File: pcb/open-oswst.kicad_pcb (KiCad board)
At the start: 2 copper layers, 70 x 50 mm, 16 parts

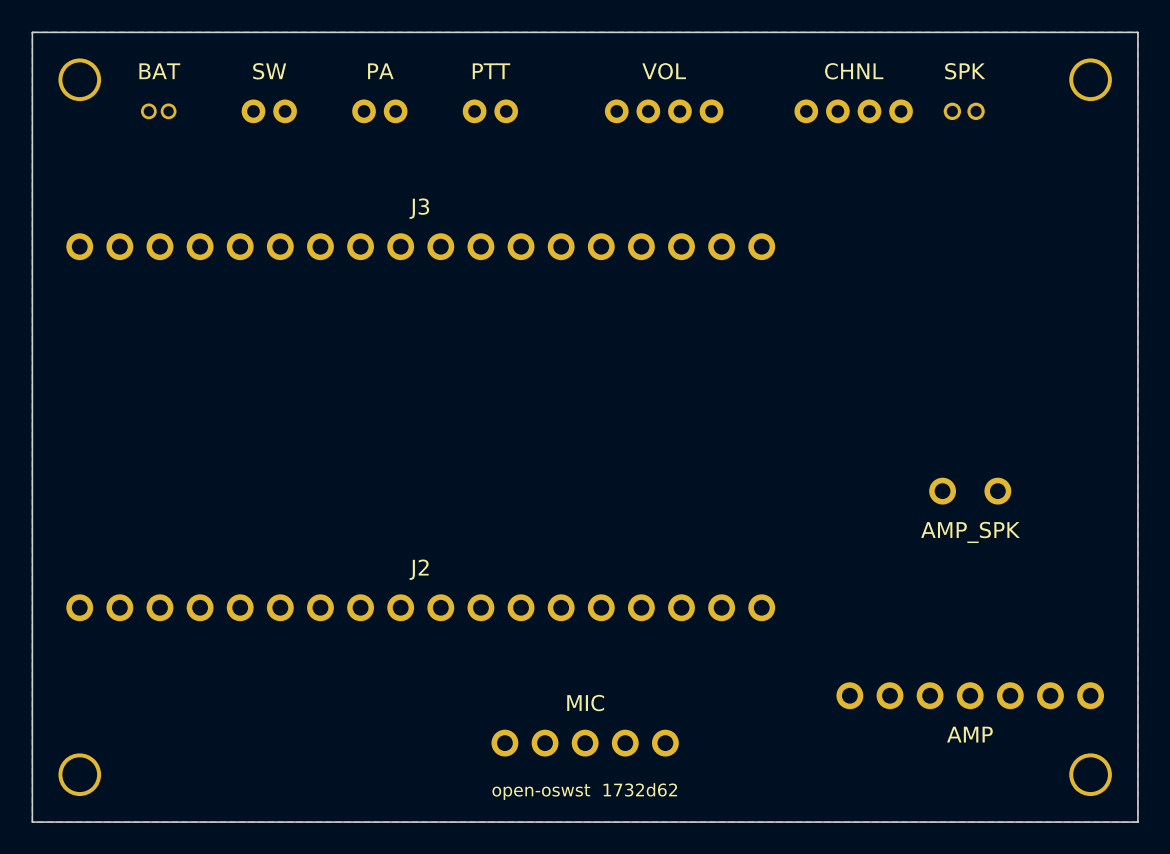
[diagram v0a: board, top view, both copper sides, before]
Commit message: PCB: fix connector types and MIC pin order
- BAT: JST-SH → JST-PH (2.0mm, standard LiPo connector)
- SPK: JST-PH → JST-ZH (1.5mm, matches speaker connector)
- Flip SPK pin order to uncross traces
- Fix MIC header pin order to match actual board (GND,VDD,GAIN,OUT,AR)
- Reduce thermal gap/bridge to 0.3mm to fix DRC spoke errors
- Add add_text() and add_jst_zh() to PCB DSL
- Switch paper to USLetter for 1:1 printing

Co-Authored-By: Claude Opus 4.6 <noreply@anthropic.com>
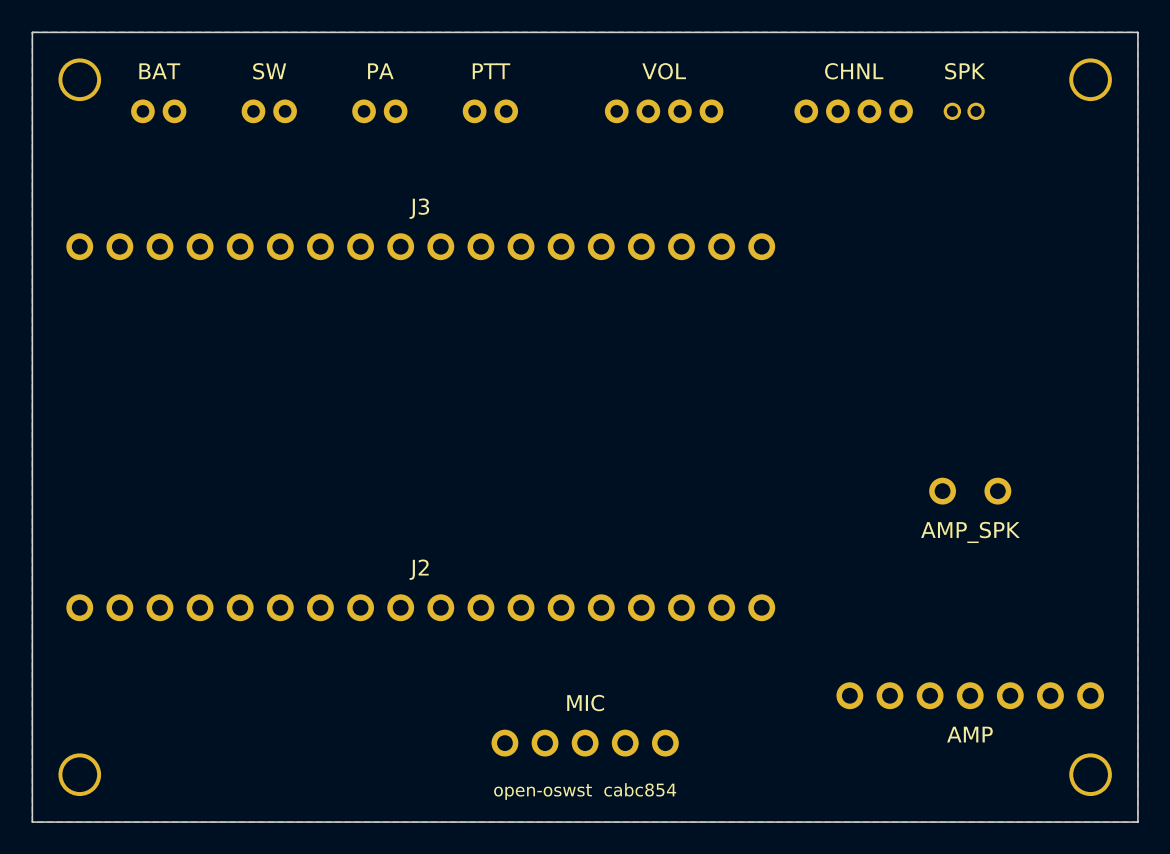
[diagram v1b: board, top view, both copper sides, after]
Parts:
- removed the BAT at (121.0, 118.0)
- added BAT: , JST_PH_B2B, F.Cu at (121.0, 118.0)
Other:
- board text added: "open-oswst cabc854"
- board text removed: "open-oswst 1732d62"
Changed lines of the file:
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@@
   )
   (gr_rect (start 113 113) (end 183 163) (stroke (width 0.1) (type solid)) (fill none) (layer "Edge.Cuts"))
-  (gr_text "open-oswst  1732d62"
+  (gr_text "open-oswst  cabc854"
     (at 148.0 161)
     (layer "F.SilkS")
@@
     )
   )
-  (footprint "JST_SH_B2B"
+  (footprint "JST_PH_B2B"
     (layer "F.Cu")
     (at 121 118)
@@
     )
     (pad "+" thru_hole circle
-      (at -0.625 0)
-      (size 1.0 1.0)
-      (drill 0.65)
+      (at -1.0 0)
+      (size 1.5 1.5)
+      (drill 0.8)
       (layers *.Cu *.Mask)
       (net 1 "VBAT")
     )
     (pad "-" thru_hole circle
-      (at 0.625 0)
-      (size 1.0 1.0)
-      (drill 0.65)
+      (at 1.0 0)
+      (size 1.5 1.5)
+      (drill 0.8)
       (layers *.Cu *.Mask)
       (net 2 "GND")
